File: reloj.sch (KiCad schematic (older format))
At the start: 81 parts, among them J1 Conn_01x03, J2 USB_B_Mini, SW1 SW_Push, SW2 SW_Push, SW3 SW_Push, U1 LM555, U10 74LS90, U11 74LS90, U12 74LS90, U13 74LS90, U14 74LS08, U15 74LS47, U16 SA04-11SRWA, U17 74LS47, U18 SA04-11SRWA, U19 74LS47, U2 CD4060B, U20 SA04-11SRWA, U21 74LS47, U22 SA04-11SRWA, U3 74LS90, U4 74LS90, U5 74LS90, U6 74LS90, U7 74LS90, U8 74LS92, U9 74LS92, Y1 32768Hz

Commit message: Added most BOM items.
Finished placement on pcb
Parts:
- added C1, C10: 0.1u, Capacitor_THT:C_Disc_D3.8mm_W2.6mm_P2.50mm, symbol Device:C_Small
- C8: renamed from C7; DKPN (none) -> 399-4220-ND‎; MPN (none) -> ‎C317C220J2G5TA‎
- C9: renamed from C8; DKPN (none) -> 399-4220-ND‎; MPN (none) -> ‎C317C220J2G5TA‎
- J2: DKPN (none) -> A135698-ND‎; MPN (none) -> ‎2172034-1‎
- R1: DKPN (none) -> CF18JT220RCT-ND‎; MPN (none) -> ‎CF18JT220R‎
- R10, R11, R12, R13, R14, R15, R16, R17, R18, R19, R20, R21, R22, R23, R24, R25, R26, R27, R28, R29, R30, R31, R32, R33, R34, R7, R8, R9: DKPN (none) -> CF18JT330RCT-ND‎; MPN (none) -> ‎CF18JT330R‎
- R2: DKPN (none) -> RNV14FAL15M0CT-ND‎; MPN (none) -> ‎RNV14FAL15M0‎
- R3: DKPN (none) -> CF18JT330KCT-ND‎; MPN (none) -> ‎CF18JT330K‎
- R4, R5, R6: DKPN (none) -> CF18JT10K0CT-ND‎; MPN (none) -> ‎CF18JT10K0‎
- RV1: footprint Potentiometer_SMD:Potentiometer_Bourns_3269X_Horizontal -> ultra_librarian:3296Y-1-102LF
- SW1, SW2, SW3: DKPN (none) -> CF18JT1K00CT-ND‎; MPN (none) -> ‎CF18JT1K00‎
- U10, U11, U12, U13, U3, U4, U5, U6, U7: DKPN (none) -> 296-34031-5-ND‎; MPN (none) -> ‎SN74LS90N‎
- U14: DKPN (none) -> 296-1633-5-ND‎; MPN (none) -> ‎SN74LS08N‎
- U15, U17, U19, U21: footprint Package_DIP:DIP-14_W7.62mm -> Package_DIP:DIP-16_W7.62mm; DKPN (none) -> 296-3712-5-ND‎; MPN (none) -> ‎SN74LS47N‎
- U16, U18, U20, U22: DKPN (none) -> 754-1457-5-ND‎; MPN (none) -> SA04-11SRWA‎
- U2: DKPN (none) -> 296-2060-ND‎; MPN (none) -> ‎CD4060BE‎
- U8, U9: DKPN (none) -> 296-26521-5-ND; MPN (none) -> ‎SN74LS92N‎
- Y1: DKPN (none) -> ‎300-1002-ND‎; MPN (none) -> CFS-20632768DZFB‎
- renumbered C9 to C11, C10 to C12, C11 to C13, C12 to C14, C13 to C15, C14 to C16, C15 to C17, C16 to C18, C17 to C19, C1 to C2, C18 to C20, C2 to C3, C3 to C4, C4 to C5, C5 to C6, C6 to C7
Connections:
- net CA: now also C1.1, C10.1
- net GND: now also C1.2, C10.2

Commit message: layout updates
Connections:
- net DM_Q2: no longer U15.6 (D)
- net DM_Q3: now also U15.6 (D)
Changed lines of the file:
@@
 DM_Q2
 Text Label 1000 7700 0    50   ~ 0
-DM_Q2
+DM_Q3
 Text Label 6600 7400 0    50   ~ 0
 DH_Q0

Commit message: Added 4.7uF cap and cleaned up traces/silkscreen
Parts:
- added C21: 4.7uF, Capacitor_THT:CP_Radial_D5.0mm_P2.00mm, symbol Device:CP1_Small
- U1: DKPN (none) -> 296-NE555P-ND; MPN (none) -> NE555P
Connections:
- net CA: now also C21.1
- net GND: now also C21.2
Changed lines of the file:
@@
 F 2 "Package_DIP:DIP-8_W7.62mm" H 2300 2100 50  0001 C CNN
 F 3 "http://www.ti.com/lit/ds/symlink/lm555.pdf" H 2300 2100 50  0001 C CNN
+F 4 "296-NE555P-ND" H 2300 2100 50  0001 C CNN "DKPN"
+F 5 "NE555P" H 2300 2100 50  0001 C CNN "MPN"
 	1    2300 2100
 	1    0    0    -1
@@
 Wire Wire Line
 	900  4800 1400 4800
-Text Label 1400 4600 2    50   ~ 0
-CLK_1HZ_ALT
 $Comp
 L Connector:USB_B_Mini J2
@@
 L power:VCC #PWR086
 U 1 1 603F37E7
-P 3900 9700
-F 0 "#PWR086" H 3900 9550 50  0001 C CNN
-F 1 "VCC" H 3917 9873 50  0000 C CNN
-F 2 "" H 3900 9700 50  0001 C CNN
-F 3 "" H 3900 9700 50  0001 C CNN
-	1    3900 9700
+P 4000 9650
+F 0 "#PWR086" H 4000 9500 50  0001 C CNN
+F 1 "VCC" H 4017 9823 50  0000 C CNN
+F 2 "" H 4000 9650 50  0001 C CNN
+F 3 "" H 4000 9650 50  0001 C CNN
+	1    4000 9650
 	1    0    0    -1
 $EndComp
 Wire Wire Line
-	3900 9700 3900 9800
+	4000 9650 4000 9800
 Wire Wire Line
-	3900 9800 3800 9800
+	4000 9800 3800 9800
 Wire Wire Line
 	3400 10400 3400 10500
@@
 Wire Wire Line
 	11700 2100 11700 2200
+$Comp
+L Device:CP1_Small C21
+U 1 1 5EAD3A17
+P 4200 10000
+F 0 "C21" H 4291 10046 50  0000 L CNN
+F 1 "4.7uF" H 4291 9955 50  0000 L CNN
+F 2 "Capacitor_THT:CP_Radial_D5.0mm_P2.00mm" H 4200 10000 50  0001 C CNN
+F 3 "~" H 4200 10000 50  0001 C CNN
+F 4 "P5308-ND" H 4200 10000 50  0001 C CNN "DKPN"
+F 5 "ECA-2AM4R7" H 4200 10000 50  0001 C CNN "MPN"
+	1    4200 10000
+	1    0    0    -1
+$EndComp
+$Comp
+L power:VCC #PWR0102
+U 1 1 5EAD5A9A
+P 4200 9700
+F 0 "#PWR0102" H 4200 9550 50  0001 C CNN
+F 1 "VCC" H 4217 9873 50  0000 C CNN
+F 2 "" H 4200 9700 50  0001 C CNN
+F 3 "" H 4200 9700 50  0001 C CNN
+	1    4200 9700
+	1    0    0    -1
+$EndComp
+$Comp
+L power:GND #PWR0103
+U 1 1 5EAD5E71
+P 4200 10250
+F 0 "#PWR0103" H 4200 10000 50  0001 C CNN
+F 1 "GND" H 4205 10077 50  0000 C CNN
+F 2 "" H 4200 10250 50  0001 C CNN
+F 3 "" H 4200 10250 50  0001 C CNN
+	1    4200 10250
+	1    0    0    -1
+$EndComp
+Wire Wire Line
+	4200 9700 4200 9900
+Wire Wire Line
+	4200 10250 4200 10100
+Text Label 4000 9800 2    50   ~ 0
+VCC
+Text Label 1400 4600 2    50   ~ 0
+CLK_1HZ_ALT
 $EndSCHEMATC

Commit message: Fixed BOM
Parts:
- SW1, SW2, SW3: DKPN CF18JT1K00CT-ND‎ -> 450-1650-ND; MPN ‎CF18JT1K00‎ -> 1825910-6
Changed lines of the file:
@@
 Sheet 1 1
 Title "Reloj"
-Date "2020-05-01"
+Date "2020-05-18"
 Rev "1.0"
 Comp "alvarop.com"
@@
 F 2 "alvarop:TE_1825910-6" H 13000 7800 50  0001 C CNN
 F 3 "~" H 13000 7800 50  0001 C CNN
-F 4 "CF18JT1K00CT-ND‎" H 13000 7600 50  0001 C CNN "DKPN"
-F 5 "‎CF18JT1K00‎" H 13000 7600 50  0001 C CNN "MPN"
+F 4 "450-1650-ND" H 13000 7600 50  0001 C CNN "DKPN"
+F 5 "1825910-6" H 13000 7600 50  0001 C CNN "MPN"
 	1    13000 7600
 	1    0    0    -1
@@
 F 2 "alvarop:TE_1825910-6" H 14100 7800 50  0001 C CNN
 F 3 "~" H 14100 7800 50  0001 C CNN
-F 4 "CF18JT1K00CT-ND‎" H 14100 7600 50  0001 C CNN "DKPN"
-F 5 "‎CF18JT1K00‎" H 14100 7600 50  0001 C CNN "MPN"
+F 4 "450-1650-ND" H 14100 7600 50  0001 C CNN "DKPN"
+F 5 "1825910-6" H 14100 7600 50  0001 C CNN "MPN"
 	1    14100 7600
 	1    0    0    -1
@@
 F 2 "alvarop:TE_1825910-6" H 15200 7800 50  0001 C CNN
 F 3 "~" H 15200 7800 50  0001 C CNN
-F 4 "CF18JT1K00CT-ND‎" H 15200 7600 50  0001 C CNN "DKPN"
-F 5 "‎CF18JT1K00‎" H 15200 7600 50  0001 C CNN "MPN"
+F 4 "450-1650-ND" H 15200 7600 50  0001 C CNN "DKPN"
+F 5 "1825910-6" H 15200 7600 50  0001 C CNN "MPN"
 	1    15200 7600
 	1    0    0    -1

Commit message: Changes for v1.1
Removed global reset button.
Connected tens of minutes and tens of second counter resets to their Q3 output via RC filter. This prevents them from resetting themselves before clocking the next device.
Reduced resistor for CLK_MIN and CLK_HR so that the buttons can still overpower it.
Moved USB connector to other side and added silkscreen note
Updated reference designators to make a bit more sense

NOTE: New resistor values aren't final
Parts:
- removed C19: 0.1u, Capacitor_THT:C_Disc_D3.8mm_W2.6mm_P2.50mm, symbol Device:C_Small
- removed SW3: SW_Push, alvarop:TE_1825910-6, symbol Switch:SW_Push
- added C12, C15: 0.1u, Capacitor_THT:C_Disc_D3.8mm_W2.6mm_P2.50mm, symbol Device:C_Small
- added R7: 330, Resistor_THT:R_Axial_DIN0204_L3.6mm_D1.6mm_P5.08mm_Horizontal, symbol Device:R_Small
- R4, R5, R6: value 10k -> 330; DKPN CF18JT10K0CT-ND‎ -> CF18JT330RCT-ND‎; MPN ‎CF18JT10K0‎ -> ‎CF18JT330R‎
- renumbered C2 to C1, C9 to C10, C15 to C16, C12 to C17, C16 to C18, C17 to C19, C1 to C2, C18 to C20, C20 to C21, C21 to C22, C10 to C8, C8 to C9, R9 to R10, R10 to R11, R11 to R12, R12 to R13, R13 to R14, R14 to R15, R15 to R16, R16 to R17, R17 to R18, R18 to R19, R19 to R20, R20 to R21, R21 to R22, R22 to R23, R23 to R24, R24 to R25, R25 to R26, R26 to R27, R27 to R28, R28 to R29, R29 to R30, R30 to R31, R31 to R32, R32 to R33, R33 to R34, R34 to R35, R7 to R8, R8 to R9, U11 to U10, U9 to U11, U14 to U13, U13 to U14, U17 to U16, U19 to U17, U21 to U18, U16 to U19, U4 to U2, U18 to U20, U20 to U21, U5 to U3, U6 to U4, U7 to U5, U2 to U6, U3 to U7, U10 to U8, U8 to U9
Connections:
- net CLK_HR: now also R5.2; no longer R5.1
- net CLK_MIN: now also R4.2; no longer R4.1
- net DM_Q3: now also R5.1, R7.2; no longer R5.2
- net GND: now also U10.2 (R0(1)), U10.3 (R0(2)), U12.2 (R0(1)), U12.3 (R0(2)), U8.2 (R0(1)), U8.3 (R0(2)), C12.2, C15.2
- net at U9.8 (Q3): now also R4.1, R6.2; no longer R4.2
- net H_RST: now reaches U13.3
- net H_RST: now also U14.2 (R0(1)), U14.3 (R0(2)); no longer R6.2
- removed net T_RST: R6.1, U10.2 (R0(1)), U10.3 (R0(2)), U11.6 (R0(1)), U11.7 (R0(2)), U12.2 (R0(1)), U12.3 (R0(2)), U14.2 (R0(1)), U14.3 (R0(2)), U8.2 (R0(1)), U8.3 (R0(2)), U9.6 (R0(1)), U9.7 (R0(2))
- new net M_RST: C12.1, R7.1, U11.6 (R0(1)), U11.7 (R0(2))
- new net S_RST: C15.1, R6.1, U9.6 (R0(1)), U9.7 (R0(2))
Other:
- moved on the sheet: C16, C17, C18

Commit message: Minor updates to v1.1
Updated 22pf cap BOM item
Re-added mounting holes
Polished a few traces

Sent out to Bay Area Circuits
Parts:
- C10, C9: DKPN 399-4220-ND‎ -> BC1005CT-ND‎; MPN ‎C317C220J2G5TA‎ -> ‎K220J15C0GF5TL2‎
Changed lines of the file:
@@
 F 2 "Capacitor_THT:C_Disc_D3.8mm_W2.6mm_P2.50mm" H 12000 2700 50  0001 C CNN
 F 3 "~" H 12000 2700 50  0001 C CNN
-F 4 "399-4220-ND‎" H 12000 2700 50  0001 C CNN "DKPN"
-F 5 " ‎C317C220J2G5TA‎ " H 12000 2700 50  0001 C CNN "MPN"
+F 4 "BC1005CT-ND‎" H 12000 2700 50  0001 C CNN "DKPN"
+F 5 "‎K220J15C0GF5TL2‎" H 12000 2700 50  0001 C CNN "MPN"
 	1    12000 2700
 	-1   0    0    1
@@
 F 2 "Capacitor_THT:C_Disc_D3.8mm_W2.6mm_P2.50mm" H 12600 2700 50  0001 C CNN
 F 3 "~" H 12600 2700 50  0001 C CNN
-F 4 "399-4220-ND‎" H 12600 2700 50  0001 C CNN "DKPN"
-F 5 " ‎C317C220J2G5TA‎ " H 12600 2700 50  0001 C CNN "MPN"
+F 4 "BC1005CT-ND‎" H 12600 2700 50  0001 C CNN "DKPN"
+F 5 "‎K220J15C0GF5TL2‎" H 12600 2700 50  0001 C CNN "MPN"
 	1    12600 2700
 	-1   0    0    1

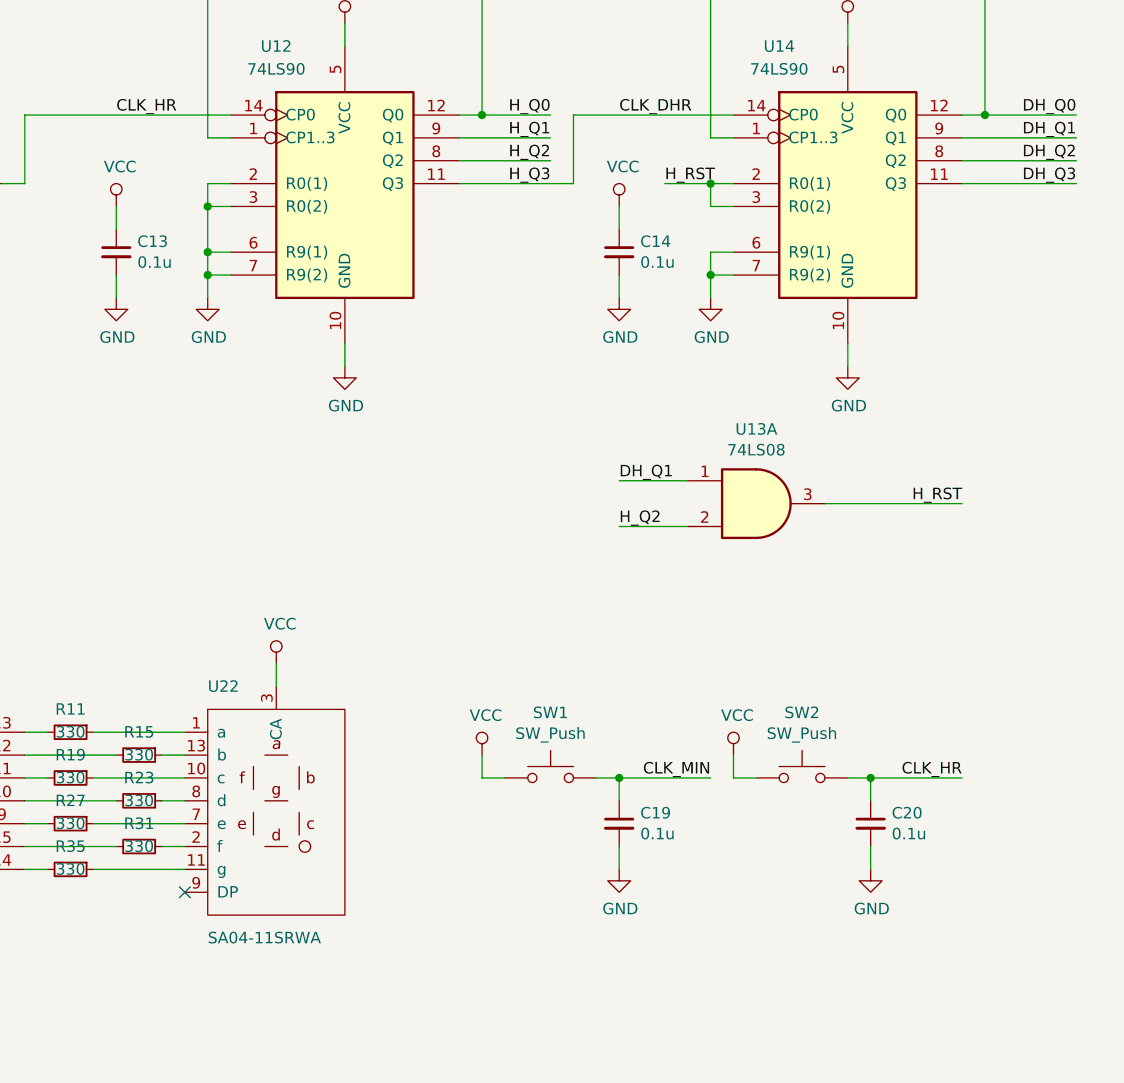
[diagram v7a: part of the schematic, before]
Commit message: Starting work on v1.2
Connected U12's R0 to H_RST. Hours were going from 23->04 since the single digit hour wasn't resetting :/

Removed both 0.1uF capacitors from CLK_MIN and CLK_HR... Not sure why they ended up there.
I'm guessing I was thinking of debouncing but they are clock lines so the IC's were behaving poorly.
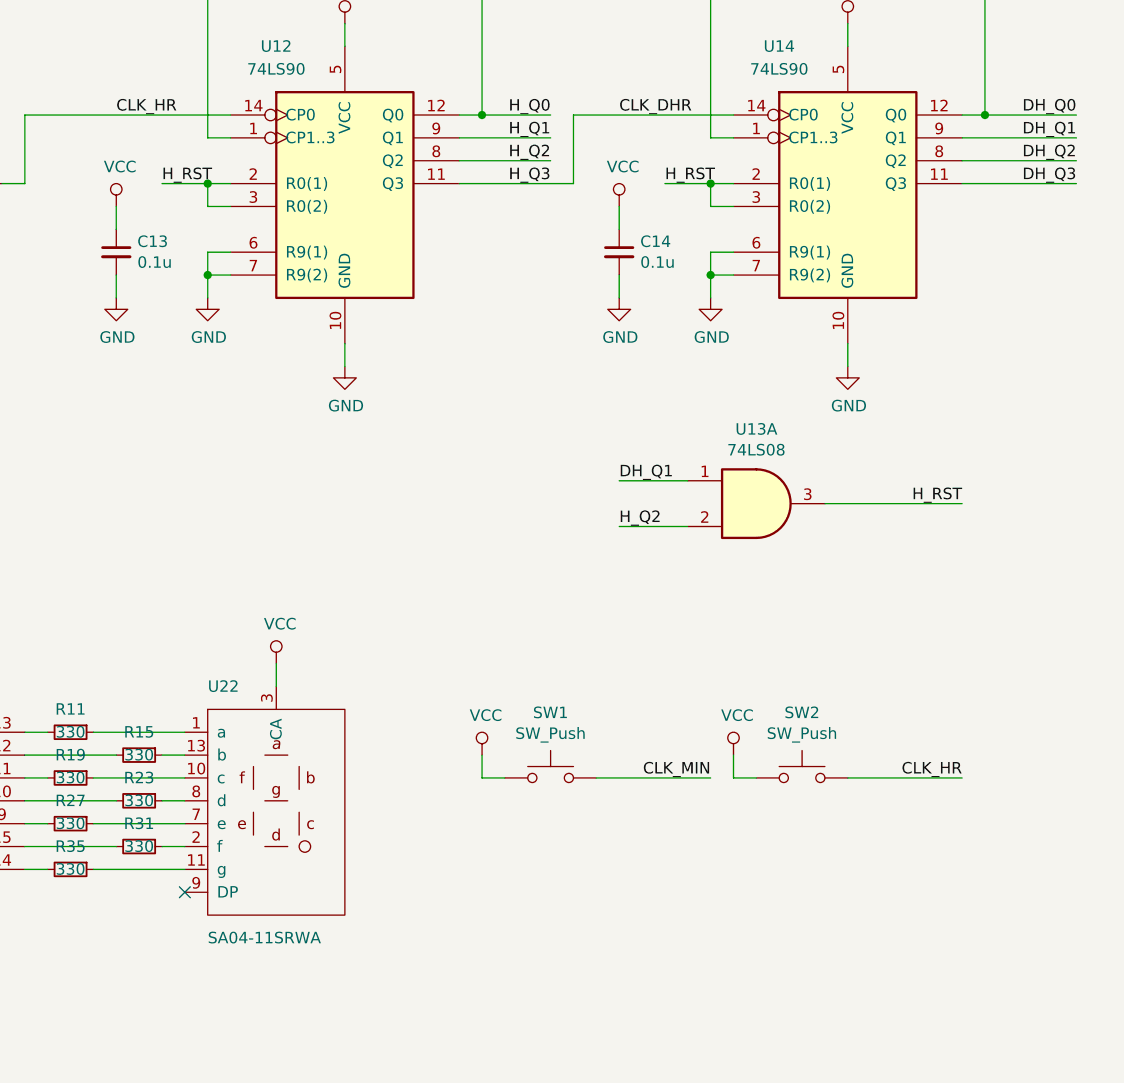
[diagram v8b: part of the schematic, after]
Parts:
- removed C19, C20: 0.1u, Capacitor_THT:C_Disc_D3.8mm_W2.6mm_P2.50mm, symbol Device:C_Small
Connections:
- net GND: no longer U12.2 (R0(1)), U12.3 (R0(2))
- net H_RST: now also U12.2 (R0(1)), U12.3 (R0(2))
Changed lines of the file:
@@
 Sheet 1 1
 Title "Reloj"
-Date "2020-05-30"
-Rev "1.1"
+Date "2020-06-05"
+Rev "1.2"
 Comp "alvarop.com"
 Comment1 ""
@@
 Wire Wire Line
 	13800 7600 13900 7600
-Wire Wire Line
-	14300 7600 14400 7600
 Text Label 14800 7600 2    50   ~ 0
 CLK_HR
-Wire Wire Line
-	13200 7600 13300 7600
 Text Label 13700 7600 2    50   ~ 0
 CLK_MIN
@@
 NoConn ~ 3800 10000
 $Comp
-L Device:C_Small C19
-U 1 1 5E7C0889
-P 13300 7800
-F 0 "C19" H 13392 7846 50  0000 L CNN
-F 1 "0.1u" H 13392 7755 50  0000 L CNN
-F 2 "Capacitor_THT:C_Disc_D3.8mm_W2.6mm_P2.50mm" H 13300 7800 50  0001 C CNN
-F 3 "~" H 13300 7800 50  0001 C CNN
-F 4 "BC3324-ND" H 13300 7800 50  0001 C CNN "DKPN"
-F 5 "K104K15X7RF53L2" H 13300 7800 50  0001 C CNN "MPN"
-	1    13300 7800
-	1    0    0    -1
-$EndComp
-Wire Wire Line
-	13300 7700 13300 7600
-Connection ~ 13300 7600
-Wire Wire Line
-	13300 7600 13700 7600
-$Comp
-L power:GND #PWR0182
-U 1 1 5E831A26
-P 13300 8000
-F 0 "#PWR0182" H 13300 7750 50  0001 C CNN
-F 1 "GND" H 13305 7827 50  0000 C CNN
-F 2 "" H 13300 8000 50  0001 C CNN
-F 3 "" H 13300 8000 50  0001 C CNN
-	1    13300 8000
-	1    0    0    -1
-$EndComp
-Wire Wire Line
-	13300 7900 13300 8000
-$Comp
-L Device:C_Small C20
-U 1 1 5E8C96CA
-P 14400 7800
-F 0 "C20" H 14492 7846 50  0000 L CNN
-F 1 "0.1u" H 14492 7755 50  0000 L CNN
-F 2 "Capacitor_THT:C_Disc_D3.8mm_W2.6mm_P2.50mm" H 14400 7800 50  0001 C CNN
-F 3 "~" H 14400 7800 50  0001 C CNN
-F 4 "BC3324-ND" H 14400 7800 50  0001 C CNN "DKPN"
-F 5 "K104K15X7RF53L2" H 14400 7800 50  0001 C CNN "MPN"
-	1    14400 7800
-	1    0    0    -1
-$EndComp
-$Comp
-L power:GND #PWR0183
-U 1 1 5E8C96D4
-P 14400 8000
-F 0 "#PWR0183" H 14400 7750 50  0001 C CNN
-F 1 "GND" H 14405 7827 50  0000 C CNN
-F 2 "" H 14400 8000 50  0001 C CNN
-F 3 "" H 14400 8000 50  0001 C CNN
-	1    14400 8000
-	1    0    0    -1
-$EndComp
-Wire Wire Line
-	14400 7900 14400 8000
-Wire Wire Line
-	14400 7700 14400 7600
-Connection ~ 14400 7600
-Wire Wire Line
-	14400 7600 14800 7600
-$Comp
 L 74xx:74LS47 U16
 U 1 1 5EBB40CA
@@
 Wire Wire Line
 	9700 5000 10300 5000
-Wire Wire Line
-	11500 5100 11500 5300
-Connection ~ 11500 5100
-Connection ~ 11500 5300
 $Comp
 L Device:C_Small C12
@@
 Connection ~ 6500 5300
 Connection ~ 6500 5100
+Wire Wire Line
+	11500 5000 11300 5000
+Connection ~ 11500 5000
+Text Label 11300 5000 0    50   ~ 0
+H_RST
+Wire Wire Line
+	13200 7600 13700 7600
+Wire Wire Line
+	14300 7600 14800 7600
 $EndSCHEMATC
